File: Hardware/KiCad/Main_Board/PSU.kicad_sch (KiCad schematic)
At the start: 3 parts, among them P1 USB_C_Plug_USB2.0

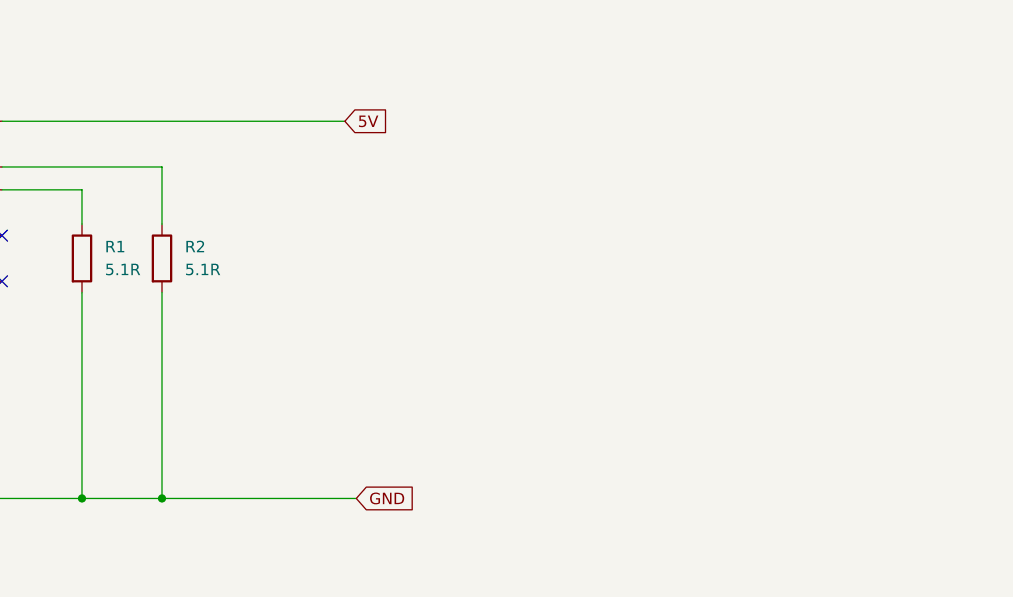
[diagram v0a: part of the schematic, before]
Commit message: New footprint based on datasheet
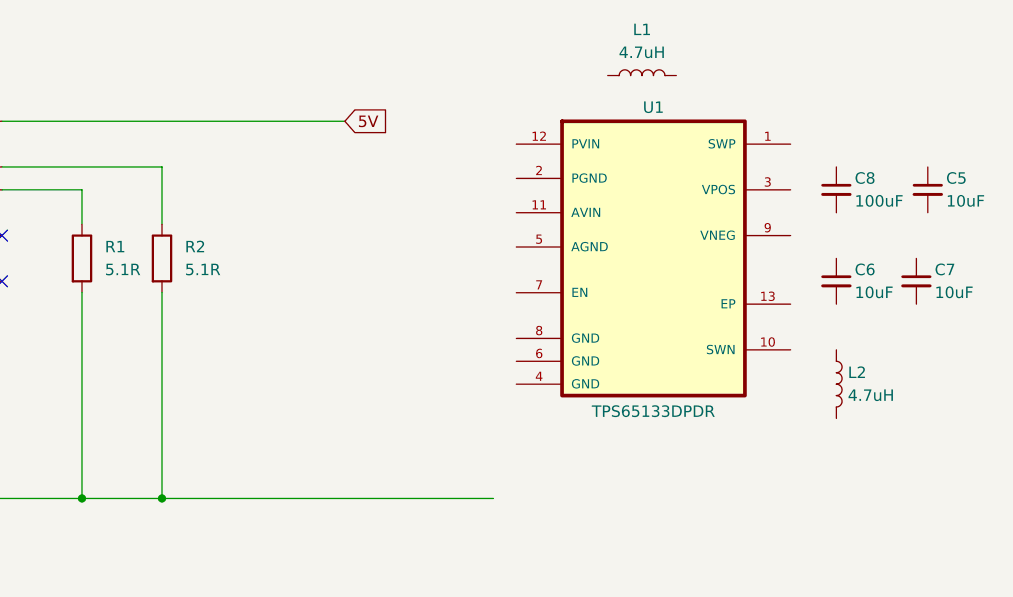
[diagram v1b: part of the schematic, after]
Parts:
- added C5, C6, C7: 10uF, SparkFun-Capacitor:C_0603_1608Metric, symbol SparkFun Capacitor:C
- added C8: 100uF, SparkFun-Capacitor:C_0603_1608Metric, symbol SparkFun Capacitor:C
- added L1, L2: 4.7uH, SparkFun-Capacitor:C_0805_2012Metric, symbol SparkFun Coil:L
- added U1: TPS65133DPDR, TPS65133DPDR:SON40P300X300X80-13N, symbol TPS65133DPDR:TPS65133DPDR

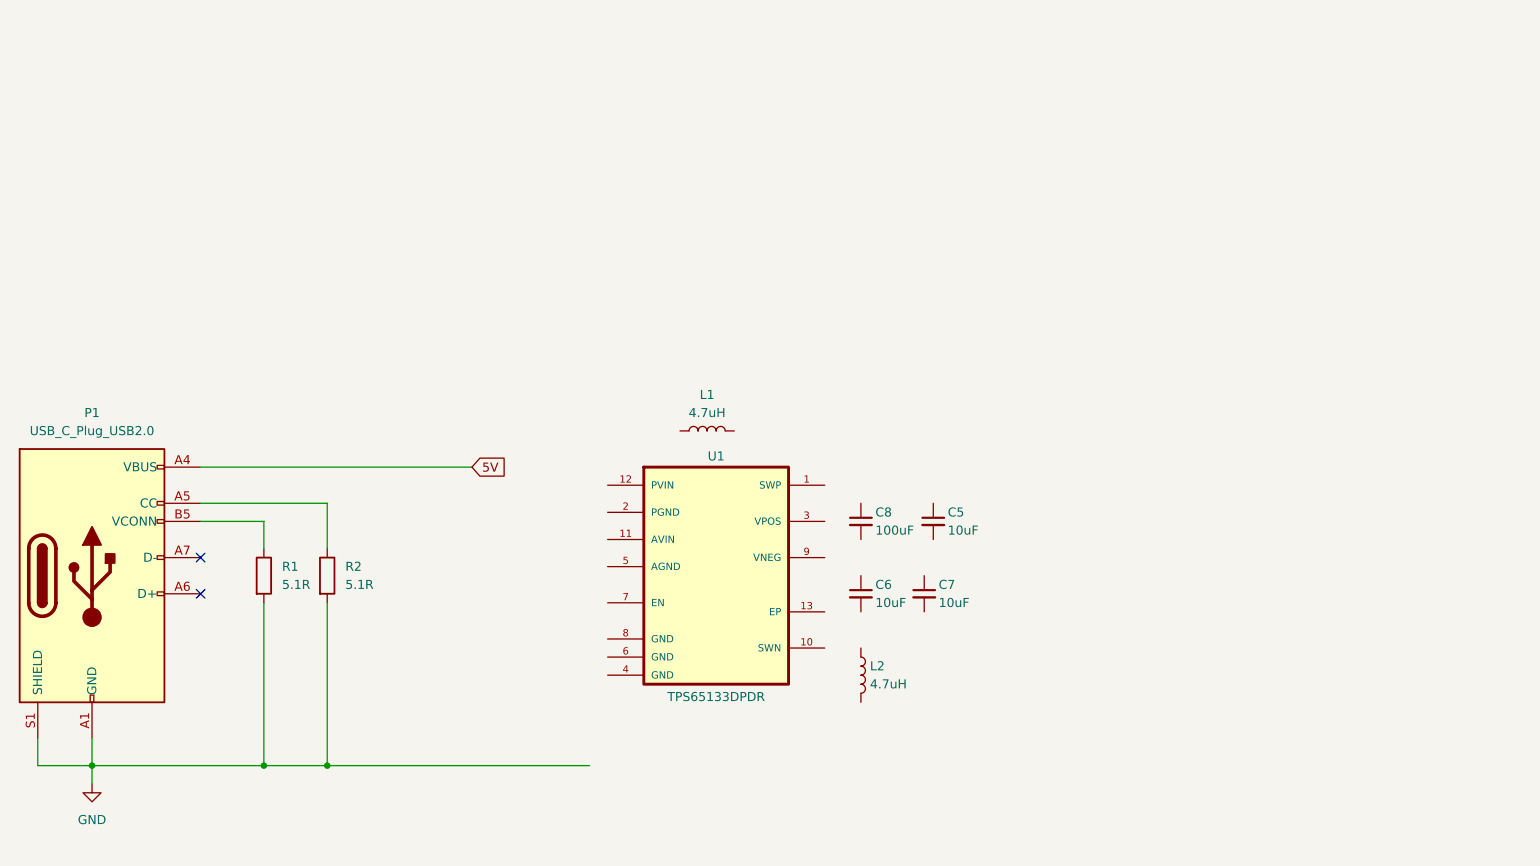
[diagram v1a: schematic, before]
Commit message: V1 PSU with double rail
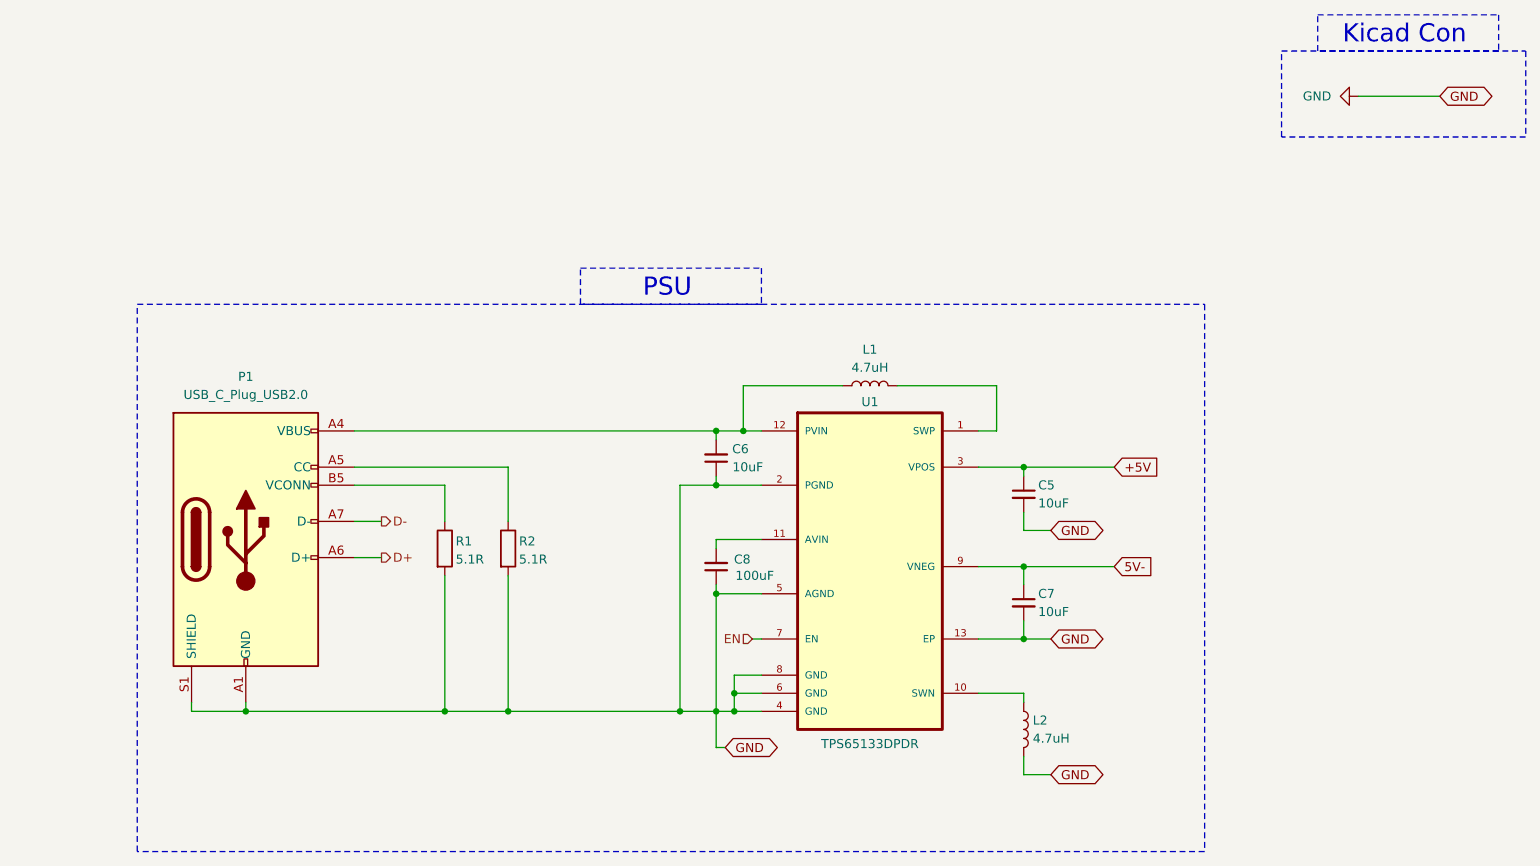
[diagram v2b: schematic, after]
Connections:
- net 5V is gone; now on an unnamed net: P1.A4 (VBUS), P1.A9 (VBUS), P1.B4 (VBUS), P1.B9 (VBUS)
- net GND: now also C5.2, C6.1, C7.2, C8.1, L2.2, U1.13 (EP), U1.2 (PGND), U1.4 (GND), U1.5 (AGND), U1.6 (GND), U1.8 (GND)
- net at L2.1: now also U1.10 (SWN)
- net 5V-: now reaches C7.1
- net 5V-: now also U1.9 (VNEG)
- net at U1.1 (SWP): now also L1.2
- net at U1.11 (AVIN): now also C8.2
- net at U1.12 (PVIN): now also C6.2, L1.1
- net +5V: now reaches U1.3 (VPOS)
- net +5V: now also C5.1
- net EN: now reaches U1.7 (EN)
- net D+: now reaches P1.A6 (D+)
- net D-: now reaches P1.A7 (D-)
- no-connect marks 2 -> 0
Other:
- note added: "Kicad Con"
- note added: "PSU"
- moved on the sheet: C5, C6, C7, C8, L1, L2, P1, R1, R2, U1
